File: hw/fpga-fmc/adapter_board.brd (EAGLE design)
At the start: 160 x 100 mm, 2 parts, among them J1 5569262-1, J2 ASP-134488-01

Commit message: fpga-fmc: add LPC pin assignment of FMC connector
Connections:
- new net FLOATING1: J2.B1
- new net FLOATING2: J2.B40
- new net FMC_CLK0_M2C_N: J2.H5
- new net FMC_CLK0_M2C_P: J2.H4
- new net FMC_CLK1_M2C_N: J2.G3
- new net FMC_CLK1_M2C_P: J2.G2
- new net FMC_DP0_C2M_N: J2.C3
- new net FMC_DP0_C2M_P: J2.C2
- new net FMC_DP0_M2C_N: J2.C7
- new net FMC_DP0_M2C_P: J2.C6
- new net FMC_GBTCLK0_M2C_N: J2.D5
- new net FMC_GBTCLK0_M2C_P: J2.D4
- new net FMC_IIC_SCL: J2.C30
- new net FMC_IIC_SDA: J2.C31
- new net FMC_LA00_CC_N: J2.G7
- new net FMC_LA00_CC_P: J2.G6
- new net FMC_LA01_CC_N: J2.D9
- new net FMC_LA01_CC_P: J2.D8
- new net FMC_LA02_N: J2.H8
- new net FMC_LA02_P: J2.H7
- new net FMC_LA03_N: J2.G10
- new net FMC_LA03_P: J2.G9
- new net FMC_LA04_N: J2.H11
- new net FMC_LA04_P: J2.H10
- new net FMC_LA05_N: J2.D12
- new net FMC_LA05_P: J2.D11
- new net FMC_LA06_N: J2.C11
- new net FMC_LA06_P: J2.C10
- new net FMC_LA07_N: J2.H14
- new net FMC_LA07_P: J2.H13
- new net FMC_LA08_N: J2.G13
- new net FMC_LA08_P: J2.G12
- new net FMC_LA09_N: J2.D15
- new net FMC_LA09_P: J2.D14
- new net FMC_LA10_N: J2.C15
- new net FMC_LA10_P: J2.C14
- new net FMC_LA11_N: J2.H17
- new net FMC_LA11_P: J2.H16
- new net FMC_LA12_N: J2.G16
- new net FMC_LA12_P: J2.G15
- new net FMC_LA13_N: J2.D18
- new net FMC_LA13_P: J2.D17
- new net FMC_LA14_N: J2.C19
- new net FMC_LA14_P: J2.C18
- new net FMC_LA15_N: J2.H20
- new net FMC_LA15_P: J2.H19
- new net FMC_LA16_N: J2.G19
- new net FMC_LA16_P: J2.G18
- new net FMC_TCK: J2.D29
- new net FMC_TDI_TDO: J2.D30, J2.D31
- new net FMC_TMS: J2.D33
- net 0V: now also J2.A1, J2.A12, J2.A13, J2.A16, J2.A17, J2.A20, J2.A21, J2.A24, J2.A25, J2.A28, J2.A29, J2.A32, J2.A33, J2.A36, J2.A37, J2.A4, J2.A40, J2.A5, J2.A8, J2.A9, J2.B10, J2.B11, J2.B14, J2.B15, J2.B18, J2.B19, J2.B2, J2.B22, J2.B23, J2.B26, J2.B27, J2.B3, J2.B30, J2.B31, J2.B34, J2.B35, J2.B38, J2.B39, J2.B6, J2.B7, J2.C1, J2.C12, J2.C13, J2.C16, J2.C17, J2.C20, J2.C21, J2.C24, J2.C25, J2.C28, J2.C29, J2.C32, J2.C33, J2.C36, J2.C38, J2.C4, J2.C40, J2.C5, J2.C8, J2.C9, J2.D10, J2.D13, J2.D16, J2.D19, J2.D2, J2.D22, J2.D25, J2.D28, J2.D3, J2.D37, J2.D39, J2.D6, J2.D7, J2.E1, J2.E11, J2.E14, J2.E17, J2.E20, J2.E23, J2.E26, J2.E29, J2.E32, J2.E35, J2.E38, J2.E4, J2.E40, J2.E5, J2.E8, J2.F12, J2.F15, J2.F18, J2.F2, J2.F21, J2.F24, J2.F27, J2.F3, J2.F30, J2.F33, J2.F36, J2.F39, J2.F6, J2.F9, J2.G1, J2.G11, J2.G14, J2.G17, J2.G20, J2.G23, J2.G26, J2.G29, J2.G32, J2.G35, J2.G38, J2.G4, J2.G40, J2.G5, J2.G8, J2.H12, J2.H15, J2.H18, J2.H2, J2.H21, J2.H24, J2.H27, J2.H3, J2.H30, J2.H33, J2.H36, J2.H39, J2.H6, J2.H9, J2.J1, J2.J11, J2.J14, J2.J17, J2.J20, J2.J23, J2.J26, J2.J29, J2.J32, J2.J35, J2.J38, J2.J4, J2.J40, J2.J5, J2.J8, J2.K12, J2.K15, J2.K18, J2.K2, J2.K21, J2.K24, J2.K27, J2.K3, J2.K30, J2.K33, J2.K36, J2.K39, J2.K6, J2.K9

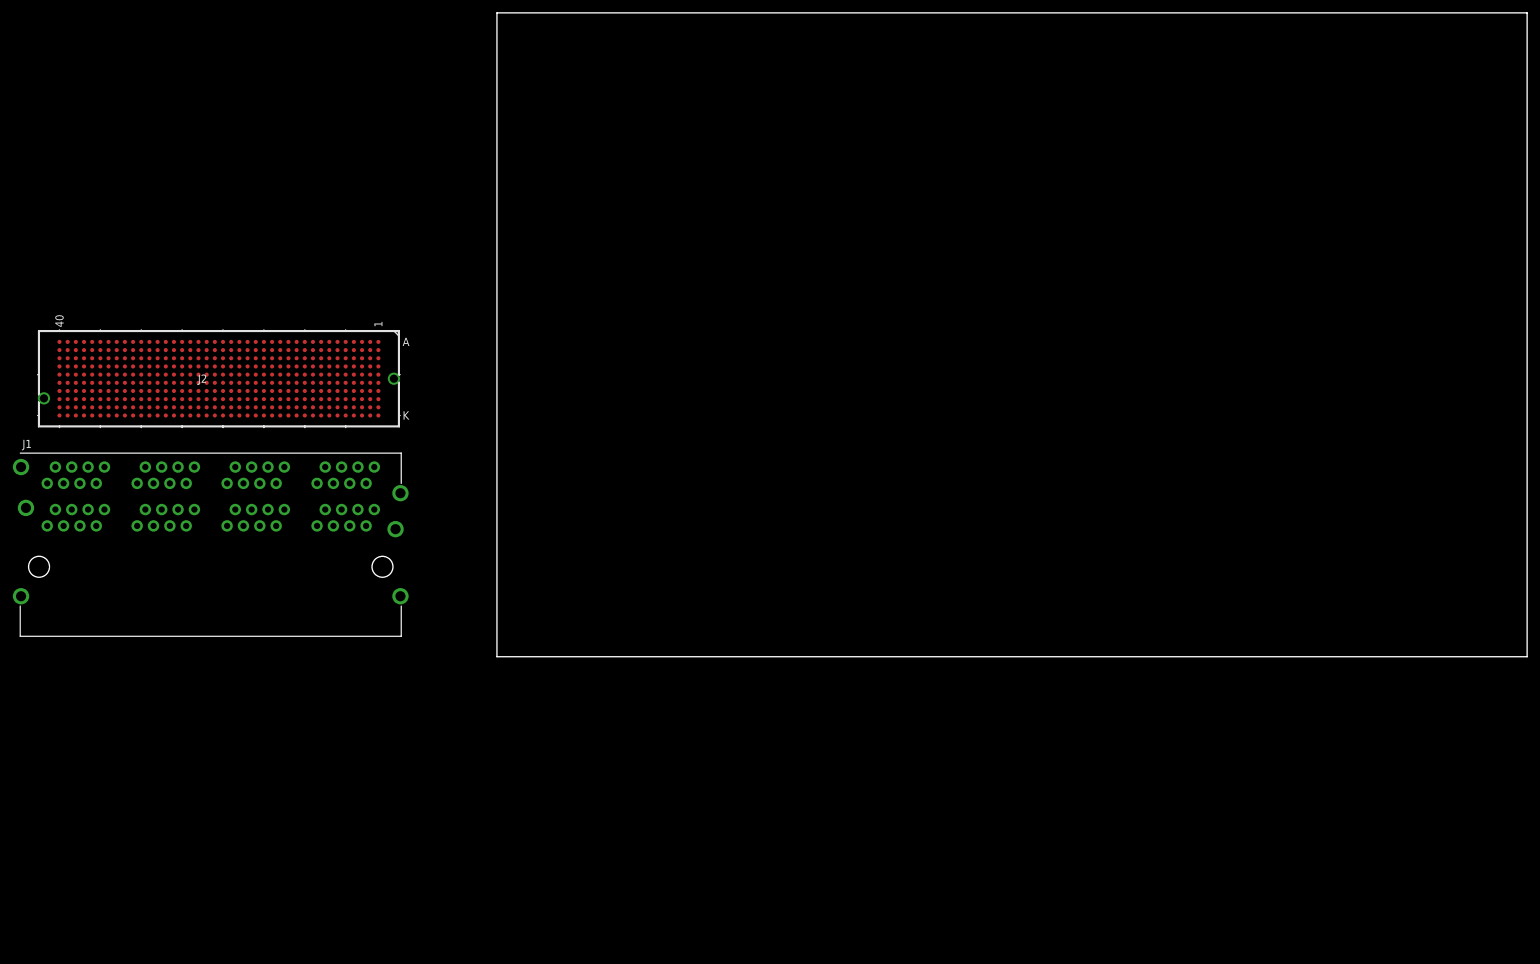
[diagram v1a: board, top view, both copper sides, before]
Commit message: fpga-fmc: fix board layout
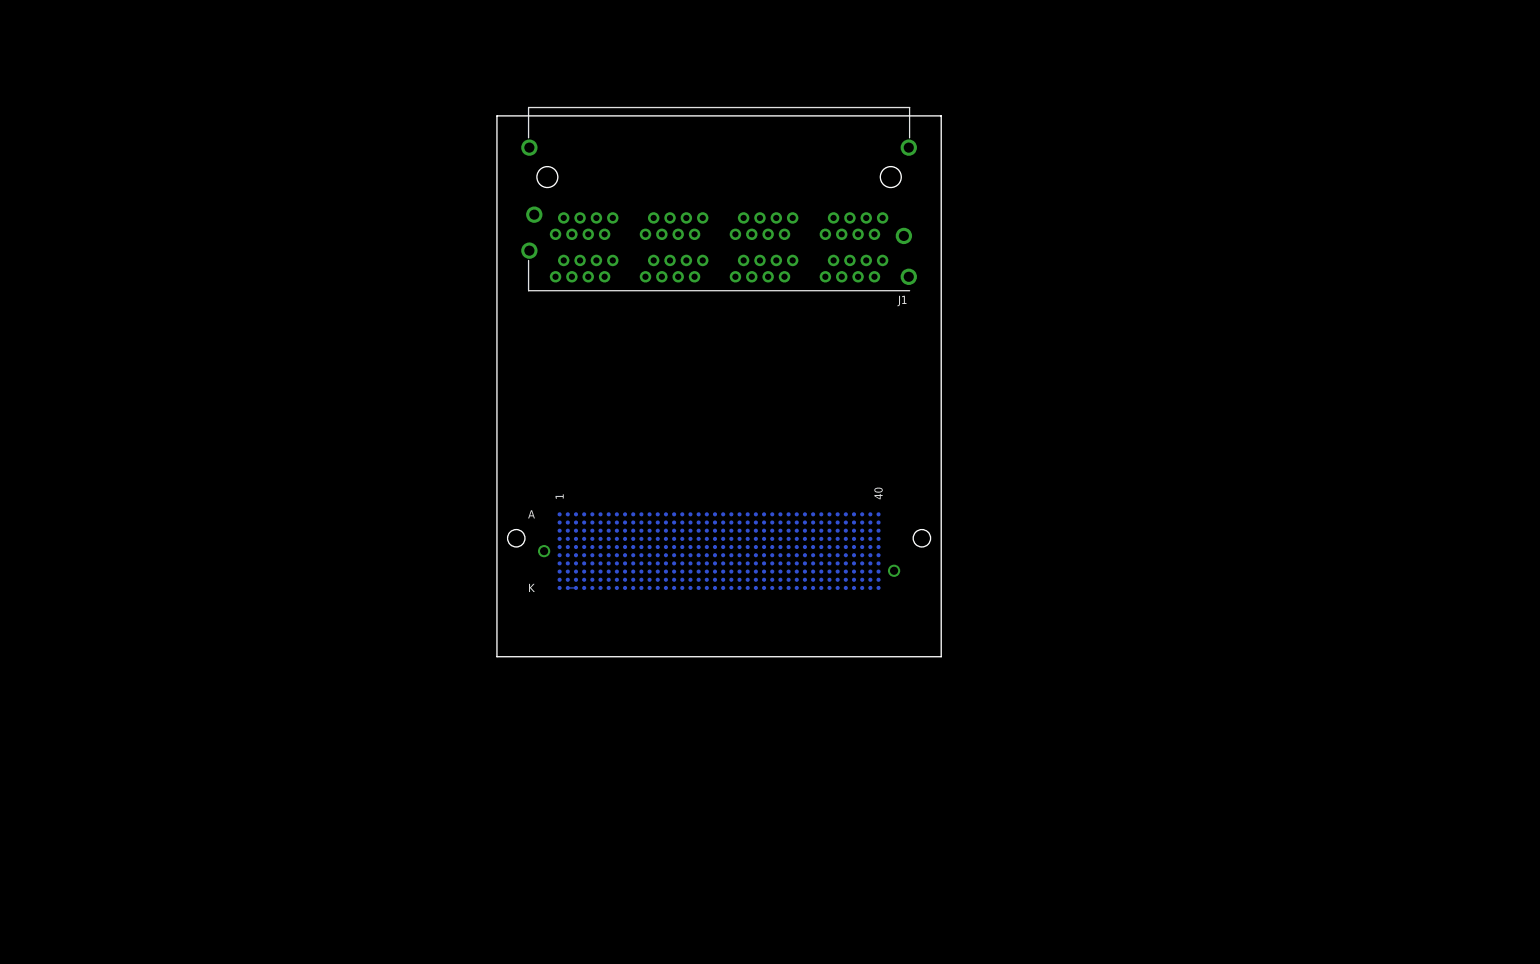
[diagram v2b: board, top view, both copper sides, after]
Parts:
- J1: device TEconnectivity_2x4_RJ45:TE_5569262-1 -> parts:TE_5569262-1
- J2: device myLib:CONN_ASP-134488-01_SAI -> parts:CONN_ASP-134488-01_SAI
- moved J1 99.5 mm to (34.5, 74.5), turned to 180 degrees
- moved J2 82.2 mm to (34.5, 16.4), flipped to the bottom
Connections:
- net CLK+1 renamed RJ1_CLK_P
- net CLK-1 renamed RJ1_CLK_N
- net CONV1 renamed RJ1_CONV
- net DATA+1 renamed RJ1_DATA_P
- net DATA-1 renamed RJ1_DATA_N
- net N$18 renamed RJ2_SDO
- net N$19 renamed RJ2_SCL
- net N$20 renamed RJ2_DATA_P
- net N$21 renamed RJ2_CONV
- net N$23 renamed RJ2_DATA_N
- net N$24 renamed RJ2_CLK_N
- net N$25 renamed RJ2_CLK_P
- net N$41 renamed RJ3_SDO
- net N$42 renamed RJ3_SCL
- net N$43 renamed RJ3_DATA_P
- net N$44 renamed RJ3_CONV
- net N$46 renamed RJ3_DATA_N
- net N$47 renamed RJ3_CLK_N
- net N$48 renamed RJ3_CLK_P
- net N$49 renamed RJ4_SDO
- net N$50 renamed RJ4_SCL
- net N$51 renamed RJ4_DATA_P
- net N$52 renamed RJ4_CONV
- net N$54 renamed RJ4_DATA_N
- net N$55 renamed RJ4_CLK_N
- net N$56 renamed RJ4_CLK_P
- net SCL1 renamed RJ1_SCL
- net SDO1 renamed RJ1_SDO
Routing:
- net 0V: track 0.00 -> 1.27 mm
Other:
- board size 160 x 100 mm -> 69 x 84 mm

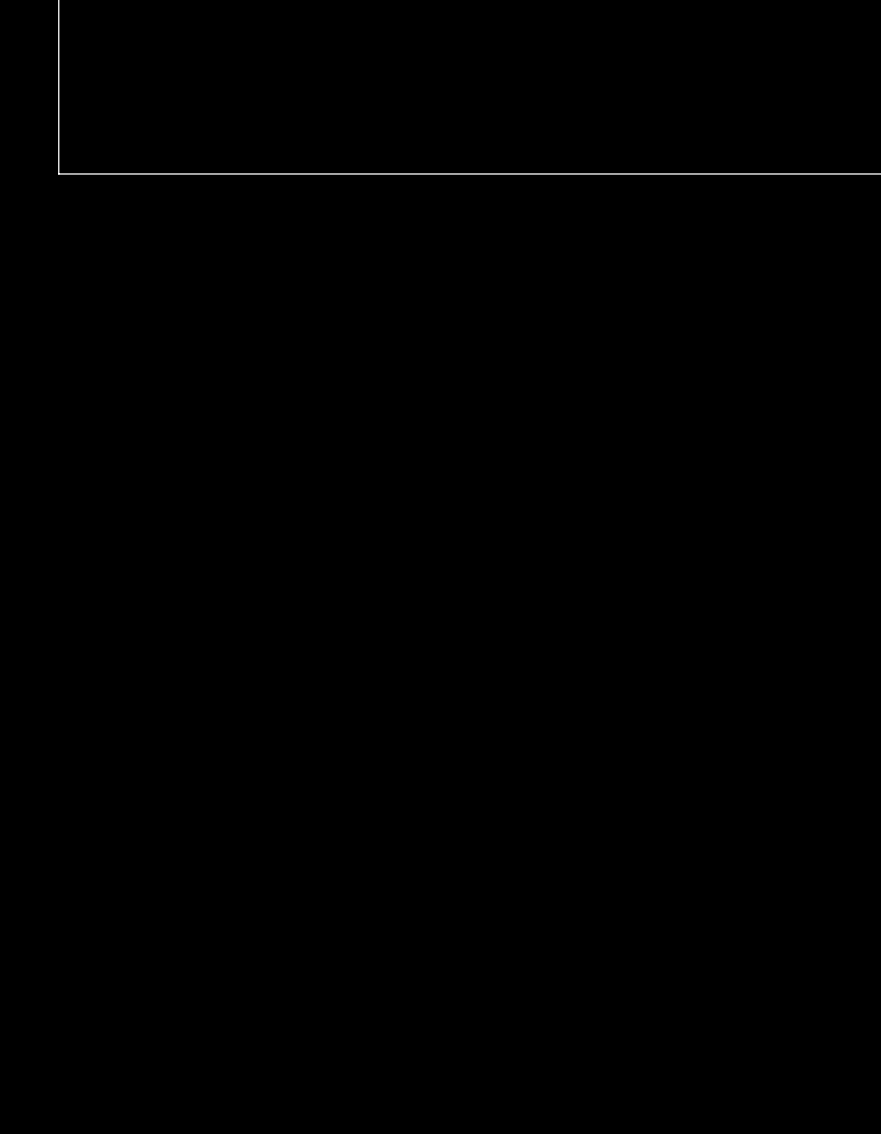
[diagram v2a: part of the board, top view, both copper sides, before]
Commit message: fpga-fmc: add devices from analog-in pcb
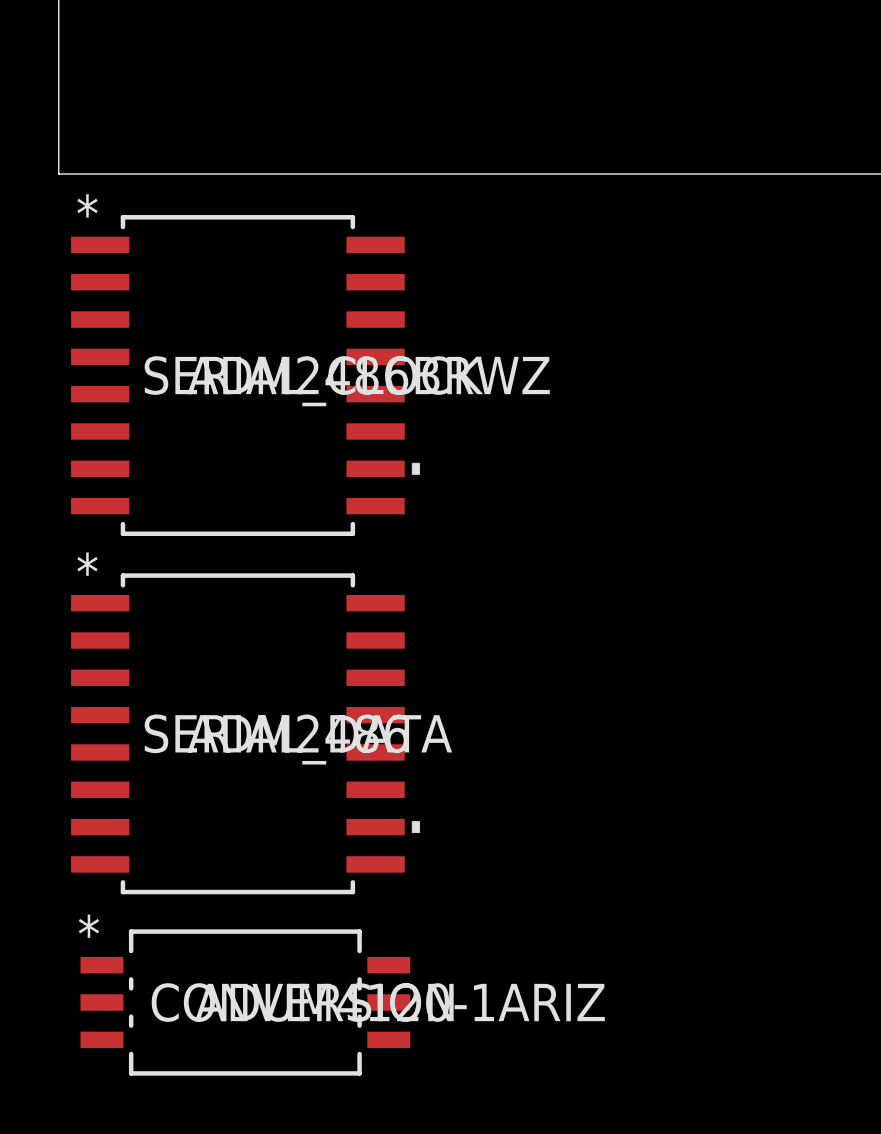
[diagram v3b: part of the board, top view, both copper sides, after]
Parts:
- added CONVERSION: ADUM4120-1ARIZ, ADUM4120:RI_6_1_ADI
- added SERIAL_CLOCK: ADM2486BRWZ, ADM2486:RW_16_ADI
- added SERIAL_DATA: ADM2486, ADM2486:RW_16_ADI
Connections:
- new net N$24: CONVERSION.5
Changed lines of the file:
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@@
 <layer number="48" name="Document" color="7" fill="1" visible="yes" active="yes"/>
 <layer number="49" name="Reference" color="7" fill="1" visible="yes" active="yes"/>
+<layer number="50" name="dxf" color="7" fill="1" visible="no" active="no"/>
 <layer number="51" name="tDocu" color="7" fill="1" visible="yes" active="yes"/>
 <layer number="52" name="bDocu" color="7" fill="1" visible="yes" active="yes"/>
+<layer number="53" name="tGND_GNDA" color="7" fill="9" visible="no" active="no"/>
+<layer number="54" name="bGND_GNDA" color="1" fill="9" visible="no" active="no"/>
+<layer number="56" name="wert" color="7" fill="1" visible="no" active="no"/>
 <layer number="88" name="SimResults" color="9" fill="1" visible="no" active="no"/>
 <layer number="89" name="SimProbes" color="9" fill="1" visible="no" active="no"/>
@@
 <layer number="97" name="Info" color="7" fill="1" visible="no" active="no"/>
 <layer number="98" name="Guide" color="6" fill="1" visible="no" active="no"/>
+<layer number="99" name="SpiceOrder" color="5" fill="1" visible="no" active="no"/>
+<layer number="100" name="Muster" color="7" fill="1" visible="no" active="no"/>
+<layer number="101" name="Patch_Top" color="12" fill="4" visible="yes" active="yes"/>
+<layer number="102" name="Vscore" color="7" fill="1" visible="yes" active="yes"/>
+<layer number="103" name="tMap" color="7" fill="1" visible="yes" active="yes"/>
+<layer number="104" name="Name" color="7" fill="1" visible="yes" active="yes"/>
+<layer number="105" name="tPlate" color="7" fill="1" visible="yes" active="yes"/>
+<layer number="106" name="bPlate" color="7" fill="1" visible="yes" active="yes"/>
+<layer number="107" name="Crop" color="7" fill="1" visible="yes" active="yes"/>
+<layer number="116" name="Patch_BOT" color="9" fill="4" visible="yes" active="yes"/>
+<layer number="121" name="_tsilk" color="7" fill="1" visible="yes" active="yes"/>
+<layer number="122" name="_bsilk" color="7" fill="1" visible="yes" active="yes"/>
+<layer number="125" name="_tNames" color="7" fill="1" visible="yes" active="yes"/>
+<layer number="144" name="Drill_legend" color="7" fill="1" visible="yes" active="yes"/>
+<layer number="151" name="HeatSink" color="7" fill="1" visible="yes" active="yes"/>
+<layer number="200" name="200bmp" color="1" fill="10" visible="yes" active="yes"/>
+<layer number="201" name="201bmp" color="2" fill="1" visible="no" active="no"/>
+<layer number="202" name="202bmp" color="3" fill="1" visible="no" active="no"/>
+<layer number="203" name="203bmp" color="4" fill="10" visible="yes" active="yes"/>
+<layer number="204" name="204bmp" color="5" fill="10" visible="yes" active="yes"/>
+<layer number="205" name="205bmp" color="6" fill="10" visible="yes" active="yes"/>
+<layer number="206" name="206bmp" color="7" fill="10" visible="yes" active="yes"/>
+<layer number="207" name="207bmp" color="8" fill="10" visible="yes" active="yes"/>
+<layer number="208" name="208bmp" color="9" fill="10" visible="yes" active="yes"/>
+<layer number="209" name="209bmp" color="7" fill="1" visible="yes" active="yes"/>
+<layer number="210" name="210bmp" color="7" fill="1" visible="yes" active="yes"/>
+<layer number="211" name="211bmp" color="7" fill="1" visible="yes" active="yes"/>
+<layer number="212" name="212bmp" color="7" fill="1" visible="yes" active="yes"/>
+<layer number="213" name="213bmp" color="7" fill="1" visible="yes" active="yes"/>
+<layer number="214" name="214bmp" color="7" fill="1" visible="yes" active="yes"/>
+<layer number="215" name="215bmp" color="7" fill="1" visible="yes" active="yes"/>
+<layer number="216" name="216bmp" color="7" fill="1" visible="yes" active="yes"/>
+<layer number="250" name="Descript" color="3" fill="1" visible="no" active="no"/>
+<layer number="251" name="SMDround" color="12" fill="11" visible="no" active="no"/>
+<layer number="254" name="cooling" color="7" fill="1" visible="yes" active="yes"/>
 </layers>
 <board>
@@
 <attribute name="NAME" x="37.7766" y="15.765" locked="yes" size="1.27" layer="26" ratio="6" rot="SMR0"/>
 <attribute name="VALUE" x="36.2272" y="15.765" locked="yes" size="1.27" layer="28" ratio="6" rot="SMR0"/>
+</element>
+<element name="SERIAL_CLOCK" library="ADM2486" package="RW_16_ADI" value="ADM2486BRWZ" x="6.096" y="-6.858" smashed="yes">
+<attribute name="BUILT_BY" value="EMA_UL_Team" x="6.096" y="-6.858" size="1.778" layer="27" display="off"/>
+<attribute name="DIGIKEY" value="ADM2486BRWZ-REELTR-ND" x="6.096" y="-6.858" size="1.778" layer="27" display="off"/>
+<attribute name="MANUFACTURER_PART_NUMBER" value="ADM2486BRWZ-REEL" x="6.096" y="-6.858" size="1.778" layer="27" display="off"/>
+<attribute name="NAME" x="2.8194" y="-7.493" size="1.27" layer="25" ratio="6" rot="SR0"/>
+<attribute name="SOURCELIBRARY" value="Analog_2012-01-01_7" x="6.096" y="-6.858" size="1.778" layer="27" display="off"/>
+<attribute name="VALUE" x="4.3688" y="-7.493" size="1.27" layer="21" ratio="6" rot="SR0"/>
+<attribute name="VENDOR" value="Analog Devices Inc" x="6.096" y="-6.858" size="1.778" layer="27" display="off"/>
+</element>
+<element name="SERIAL_DATA" library="ADM2486" package="RW_16_ADI" value="ADM2486" x="6.096" y="-19.05" smashed="yes">
+<attribute name="BUILT_BY" value="EMA_UL_Team" x="6.096" y="-19.05" size="1.778" layer="27" display="off"/>
+<attribute name="DIGIKEY" value="ADM2486BRWZ-REELTR-ND" x="6.096" y="-19.05" size="1.778" layer="27" display="off"/>
+<attribute name="MANUFACTURER_PART_NUMBER" value="ADM2486BRWZ-REEL" x="6.096" y="-19.05" size="1.778" layer="27" display="off"/>
+<attribute name="NAME" x="2.8194" y="-19.685" size="1.27" layer="25" ratio="6" rot="SR0"/>
+<attribute name="SOURCELIBRARY" value="Analog_2012-01-01_7" x="6.096" y="-19.05" size="1.778" layer="27" display="off"/>
+<attribute name="VALUE" x="4.3688" y="-19.685" size="1.27" layer="21" ratio="6" rot="SR0"/>
+<attribute name="VENDOR" value="Analog Devices Inc" x="6.096" y="-19.05" size="1.778" layer="27" display="off"/>
+</element>
+<element name="CONVERSION" library="ADUM4120" package="RI_6_1_ADI" value="ADUM4120-1ARIZ" x="6.35" y="-28.194" smashed="yes">
+<attribute name="BUILT_BY" value="Analog Devices Inc." x="6.35" y="-28.194" size="1.778" layer="27" display="off"/>
+<attribute name="DIGIKEY" value="ADUM4120-1ARIZ-ND" x="6.35" y="-28.194" size="1.778" layer="27" display="off"/>
+<attribute name="MANUFACTURER_PART_NUMBER" value="ADUM4120-1ARIZ" x="6.35" y="-28.194" size="1.778" layer="27" display="off"/>
+<attribute name="NAME" x="3.0734" y="-28.829" size="1.27" layer="25" ratio="6" rot="SR0"/>
+<attribute name="SOURCELIBRARY" value="Analog_2017-10-24" x="6.35" y="-28.194" size="1.778" layer="27" display="off"/>
+<attribute name="VALUE" x="4.6228" y="-28.829" size="1.27" layer="21" ratio="6" rot="SR0"/>
+<attribute name="VENDOR" value="Analog Devices Inc" x="6.35" y="-28.194" size="1.778" layer="27" display="off"/>
 </element>
 </elements>
@@
 <contactref element="J1" pad="1.6"/>
 </signal>
+<signal name="N$24">
+<contactref element="CONVERSION" pad="5"/>
+</signal>
 </signals>
